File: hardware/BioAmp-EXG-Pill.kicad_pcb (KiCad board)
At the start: 2 copper layers, 25.4 x 10 mm, 30 parts, among them J1 BioAmp Output, J2 BioAmp Input, U1 TL074, U2 LOGO_UDLABS

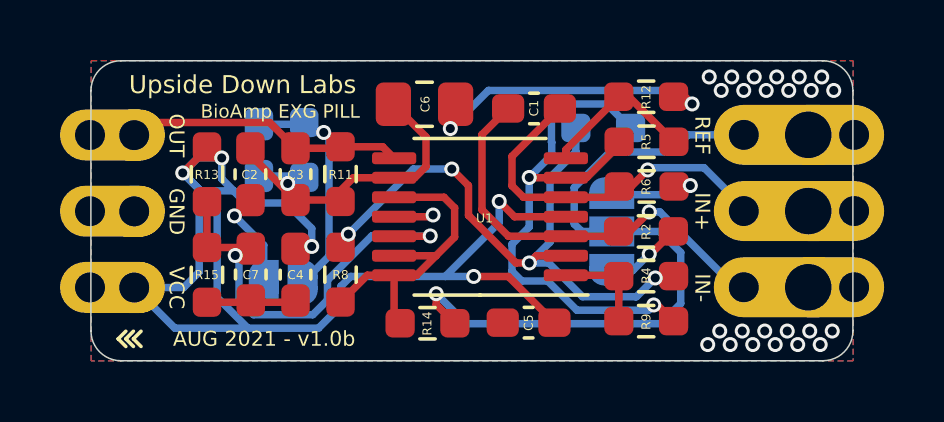
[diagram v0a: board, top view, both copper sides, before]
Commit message: redesigned PCB for manufacture MedTech style
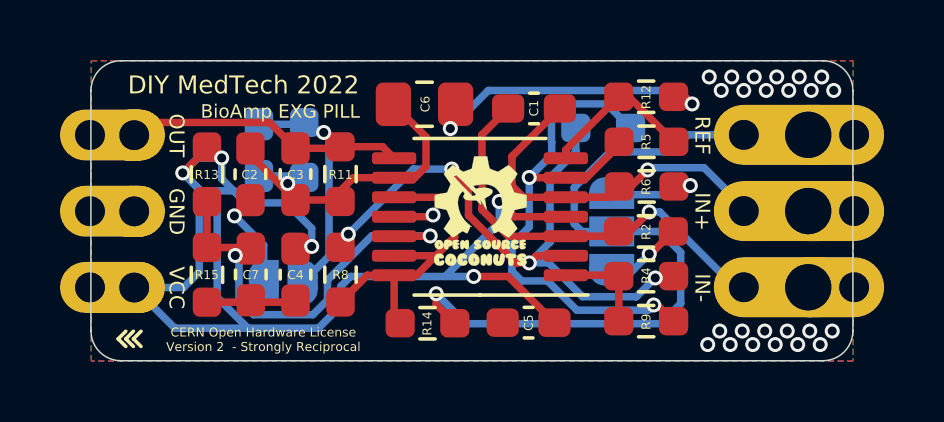
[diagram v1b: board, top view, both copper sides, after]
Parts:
- added Ref**: Val**, BioAmp:Coconut_logo, F.Cu at (123.9, 94.6)
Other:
- board text added: "CERN Open Hardware License Version 2 - Strongly Reciprocal"
- board text added: "DIY MedTech 2022"
- board text removed: "AUG 2021 - v1.0b"
- board text removed: "Upside Down Labs"
